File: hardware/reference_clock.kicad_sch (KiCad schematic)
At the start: 19 parts, among them U10 74AUP1G04, U11 Si570, U12 PL133-27GC-R, U13 PL133-27GC-R

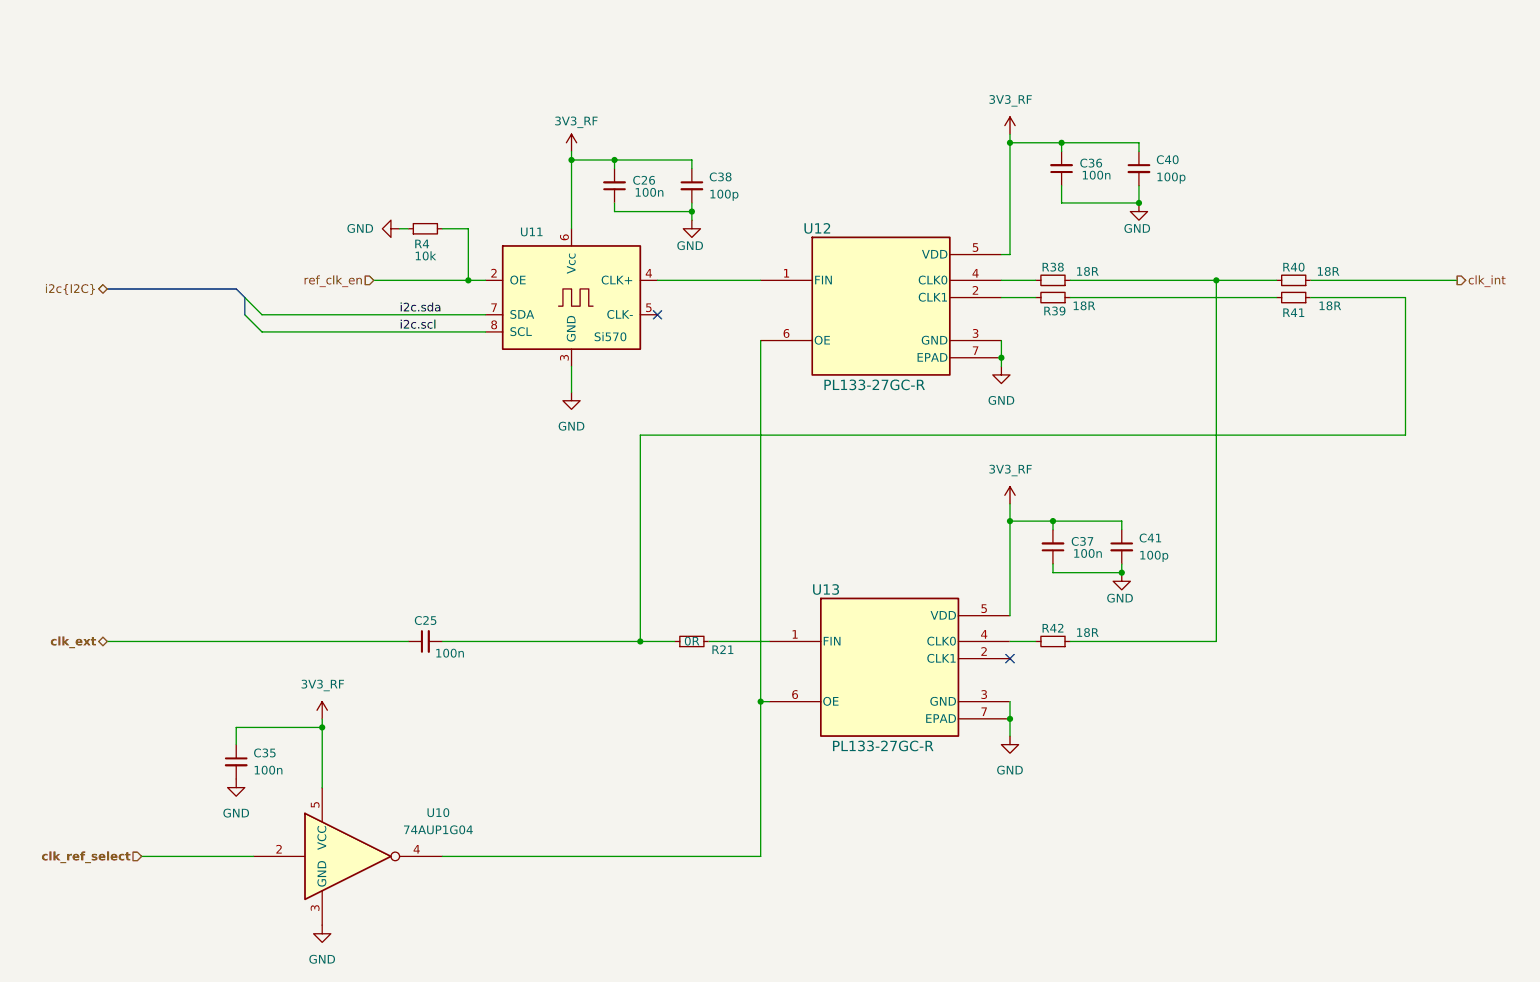
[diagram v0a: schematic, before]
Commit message: Completed core PCB routing
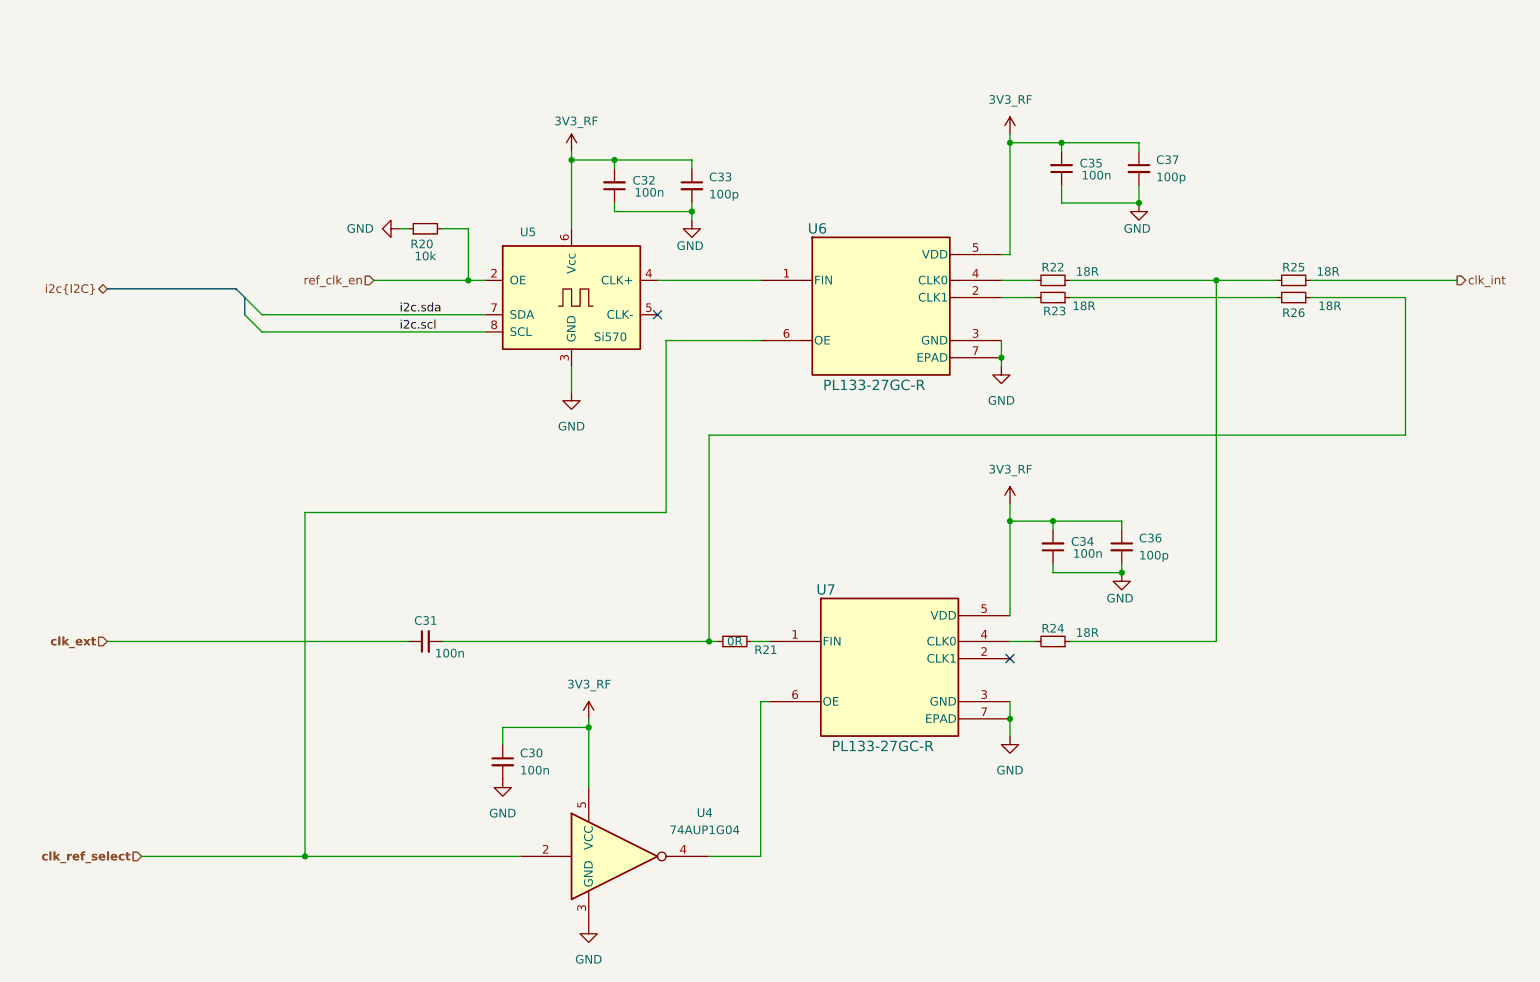
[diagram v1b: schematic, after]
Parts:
- U6: renamed from U12; footprint rf-synth-alpha:TDFN2013-6LD-PL-1_MCH -> sigma0_Package_DFN:TDFN2013-6LD-PL-1_MCH
- U7: renamed from U13; footprint rf-synth-alpha:TDFN2013-6LD-PL-1_MCH -> sigma0_Package_DFN:TDFN2013-6LD-PL-1_MCH
- renumbered C35 to C30, C25 to C31, C26 to C32, C38 to C33, C37 to C34, C36 to C35, C41 to C36, C40 to C37, R4 to R20, R38 to R22, R39 to R23, R42 to R24, R40 to R25, R41 to R26, U10 to U4, U11 to U5
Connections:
- net clk_ref_select: now also U6.6 (OE)
- net at U4.4, U7.6 (OE): no longer U6.6 (OE)
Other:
- moved on the sheet: C30, R21, U4

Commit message: Ready for FAB info
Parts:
- added C38: 100n, Capacitor_SMD:C_0402_1005Metric, symbol Device:C_Small
- added C39: 1u, Capacitor_SMD:C_0402_1005Metric, symbol Device:C_Small
- added FB4: 180R, Inductor_SMD:L_0402_1005Metric, symbol Device:FerriteBead_Small
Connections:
- net GND: now also C38.1, C39.2
- net 3V3_RF renamed 3V3_OSC
- net 3V3_OSC: now also FB4.2
- net i2c.scl renamed i2c0.scl
- net i2c.sda renamed i2c0.sda
- new net 3V3: C38.2, C39.1, FB4.1

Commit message: Sent off for quote
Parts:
- C30: MPN 04025C104JAT2A -> CL05B104KA5NNNC; Manufacturer KYOCERA AVX -> Samsung Electro-Mechanics; Supplier Mouser -> Digikey
- R21: MPN (none) -> ERJ-2GE0R00X
- U4: Manufacturer TI -> Texus Instruments
- U5: MPN (none) -> 570CAC000121DG; Manufacturer (none) -> Skyworks Solutions Inc.; SPN (none) -> 336-2519-ND; Supplier (none) -> Digikey
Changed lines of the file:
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@@
 			)
 		)
-		(property "Description" "Resistor, small symbol"
+		(property "Description" "RES SMD 0 OHM JUMPER 1/10W 0402"
 			(at 139.7 119.38 0)
 			(effects
@@
 		(property "DATE" ""
 			(at 139.7 119.38 0)
+			(effects
+				(font
+					(size 1.27 1.27)
+				)
+				(hide yes)
+			)
+		)
+		(property "MPN" "ERJ-2GE0R00X"
+			(at 139.7 122.682 90)
 			(effects
 				(font
@@
 			)
 		)
-		(property "Description" "10 MHZ TO 1.4 GHZ I2C PROGRAMMABLE XO/VCXO"
+		(property "Description" "XTAL OSC XO 100.0000MHZ CMOS SMD"
 			(at 115.57 68.58 0)
+			(effects
+				(font
+					(size 1.27 1.27)
+				)
+				(hide yes)
+			)
+		)
+		(property "MPN" "570CAC000121DG"
+			(at 103.886 78.232 0)
+			(effects
+				(font
+					(size 1.27 1.27)
+				)
+			)
+		)
+		(property "Manufacturer" "Skyworks Solutions Inc."
+			(at 103.124 90.17 0)
+			(effects
+				(font
+					(size 1.27 1.27)
+				)
+				(hide yes)
+			)
+		)
+		(property "SPN" "336-2519-ND"
+			(at 100.33 85.09 0)
+			(effects
+				(font
+					(size 1.27 1.27)
+				)
+				(hide yes)
+			)
+		)
+		(property "Supplier" "Digikey"
+			(at 98.552 87.884 0)
 			(effects
 				(font
@@
 			)
 		)
-		(property "Description" "Unpolarized capacitor, small symbol"
+		(property "Description" "CAP CER 0.1UF 25V X7R 0402"
 			(at 105.41 137.16 0)
 			(effects
@@
 			)
 		)
-		(property "Manufacturer" "KYOCERA AVX"
+		(property "Manufacturer" "Samsung Electro-Mechanics"
 			(at 105.41 137.16 0)
 			(effects
@@
 			)
 		)
-		(property "MPN" "04025C104JAT2A"
+		(property "MPN" "CL05B104KA5NNNC"
 			(at 105.41 137.16 0)
 			(effects
@@
 			)
 		)
-		(property "Supplier" "Mouser"
+		(property "Supplier" "Digikey"
 			(at 105.41 137.16 0)
 			(effects
@@
 			)
 		)
-		(property "Manufacturer" "TI"
+		(property "Manufacturer" "Texus Instruments"
 			(at 123.19 151.13 0)
 			(effects
